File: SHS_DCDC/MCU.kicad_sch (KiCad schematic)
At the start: 35 parts, among them J3 Conn_ARM_JTAG_SWD_10, J4 0022232041, J5 640456-2, SW1 TACT_SW, SW2 TACT_SW, SW3 TACT_SW, SW4 TACT_SW, SW5 TACT_SW, U8 MIC5501-3.0YM5, Y1 2-SMD no lead

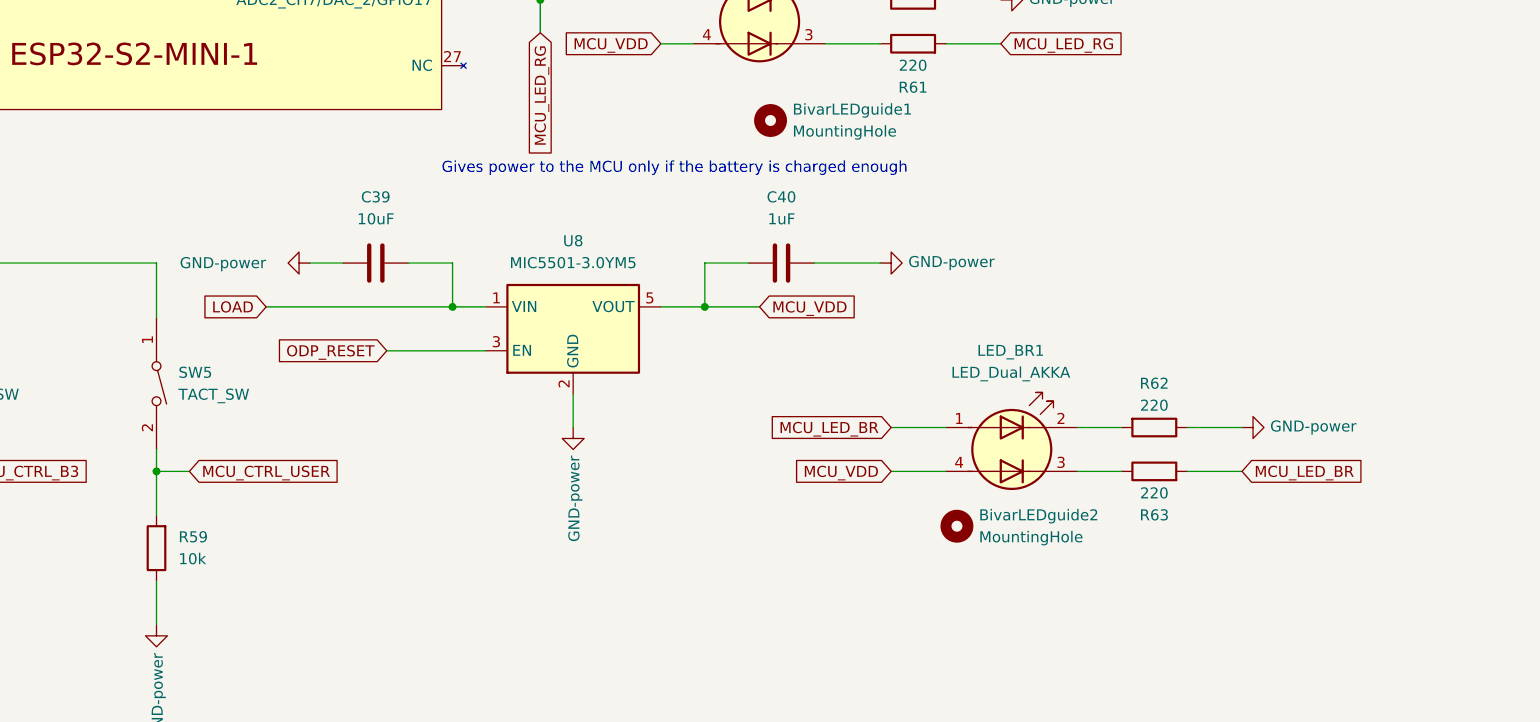
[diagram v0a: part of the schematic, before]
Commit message: Commit before reannotation
Plan to test the reannotation feature.
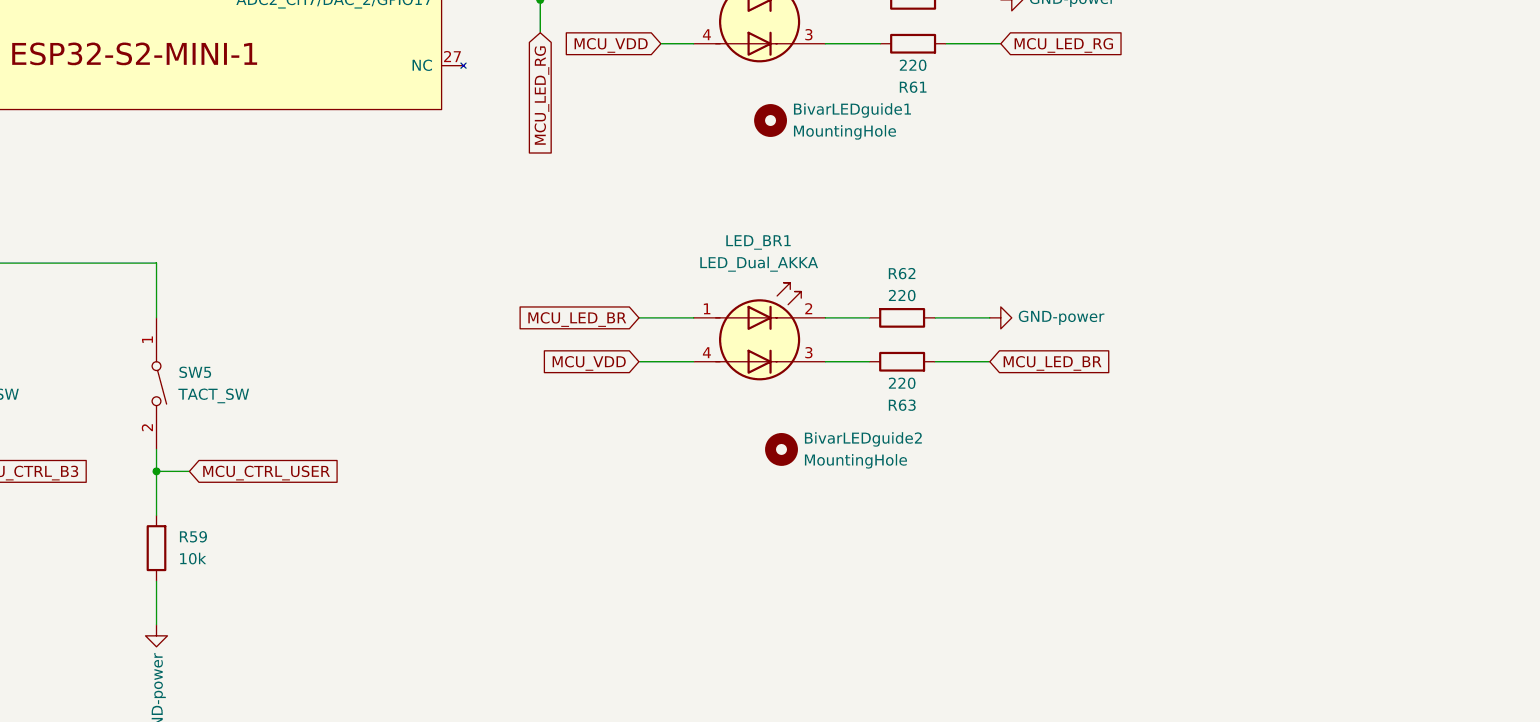
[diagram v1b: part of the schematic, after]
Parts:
- removed C39: 10uF, Capacitor_SMD:C_0805_2012Metric, symbol Device:C
- removed C40: 1uF, Capacitor_SMD:C_0603_1608Metric, symbol Device:C
- removed U8: MIC5501-3.0YM5, Package_TO_SOT_SMD:SOT-23-5, symbol Regulator_Linear:MIC5501-3.0YM5
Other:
- note removed: "Gives power to the MCU only if the battery is charged enough"
- moved on the sheet: BivarLEDguide2, LED_BR1, R62, R63

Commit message: Testpoints
All the tests points have been placed
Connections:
- net MCU_OCP_BAT is gone; now on net MCU_INA181_VDD: ESP32.5 (GPIO1/ADC1_CH0)
- net MCU_INA181_VDD: no longer ESP32.22 (ADC2_CH6/DAC_1/GPIO18)
- net MCU_5V_EN renamed MCU_USB_EN
- new net MCU_USB_ILIM: ESP32.22 (ADC2_CH6/DAC_1/GPIO18)
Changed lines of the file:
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@@
+    (stroke (width 0) (type default) (color 0 0 0 0))
+  )
+  (wire (pts (xy 80.01 36.83) (xy 90.17 36.83))
     (stroke (width 0) (type default) (color 0 0 0 0))
   )
@@
     (stroke (width 0) (type default) (color 0 0 0 0))
   )
-  (wire (pts (xy 162.56 99.06) (xy 163.83 99.06))
+  (wire (pts (xy 162.56 99.06) (xy 175.26 99.06))
     (stroke (width 0) (type default) (color 0 0 0 0))
   )
@@
   )
   (wire (pts (xy 270.51 33.02) (xy 273.05 33.02))
-    (stroke (width 0) (type default) (color 0 0 0 0))
-  )
-  (wire (pts (xy 80.01 36.83) (xy 90.17 36.83))
     (stroke (width 0) (type default) (color 0 0 0 0))
   )
@@
     )
   )
-  (global_label "MCU_INA181_VDD" (shape input) (at 163.83 99.06 0) (fields_autoplaced)
-    (effects (font (size 1.27 1.27)) (justify left))
-    (property "Intersheet References" "${INTERSHEET_REFS}" (id 0) (at 182.4223 99.1394 0)
-      (effects (font (size 1.27 1.27)) (justify left) hide)
+  (global_label "MCU_INA181_VDD" (shape input) (at 80.01 36.83 180) (fields_autoplaced)
+    (effects (font (size 1.27 1.27)) (justify right))
+    (property "Intersheet References" "${INTERSHEET_REFS}" (id 0) (at 61.4177 36.7506 0)
+      (effects (font (size 1.27 1.27)) (justify right) hide)
     )
   )
@@
     )
   )
-  (global_label "MCU_5V_EN" (shape input) (at 80.01 67.31 180) (fields_autoplaced)
-    (effects (font (size 1.27 1.27)) (justify right))
-    (property "Intersheet References" "${INTERSHEET_REFS}" (id 0) (at 66.921 67.2306 0)
+  (global_label "MCU_USB_EN" (shape input) (at 80.01 67.31 180) (fields_autoplaced)
+    (effects (font (size 1.27 1.27)) (justify right))
+    (property "Intersheet References" "${INTERSHEET_REFS}" (id 0) (at 65.4091 67.2306 0)
       (effects (font (size 1.27 1.27)) (justify right) hide)
     )
@@
     )
   )
+  (global_label "MCU_USB_ILIM" (shape input) (at 175.26 99.06 0) (fields_autoplaced)
+    (effects (font (size 1.27 1.27)) (justify left))
+    (property "Intersheet References" "${INTERSHEET_REFS}" (id 0) (at 191.0704 98.9806 0)
+      (effects (font (size 1.27 1.27)) (justify left) hide)
+    )
+  )
   (global_label "MCU_ADC_BAT_CTRL" (shape input) (at 80.01 41.91 180) (fields_autoplaced)
     (effects (font (size 1.27 1.27)) (justify right))
@@
     )
   )
-  (global_label "MCU_OCP_BAT" (shape input) (at 80.01 36.83 180) (fields_autoplaced)
-    (effects (font (size 1.27 1.27)) (justify right))
-    (property "Intersheet References" "${INTERSHEET_REFS}" (id 0) (at 64.502 36.7506 0)
-      (effects (font (size 1.27 1.27)) (justify right) hide)
-    )
-  )
